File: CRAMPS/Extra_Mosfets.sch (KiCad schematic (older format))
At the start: 12 parts, among them P901 D12, P902 D2, Q901 DMN2075U, Q902 DMN2075U

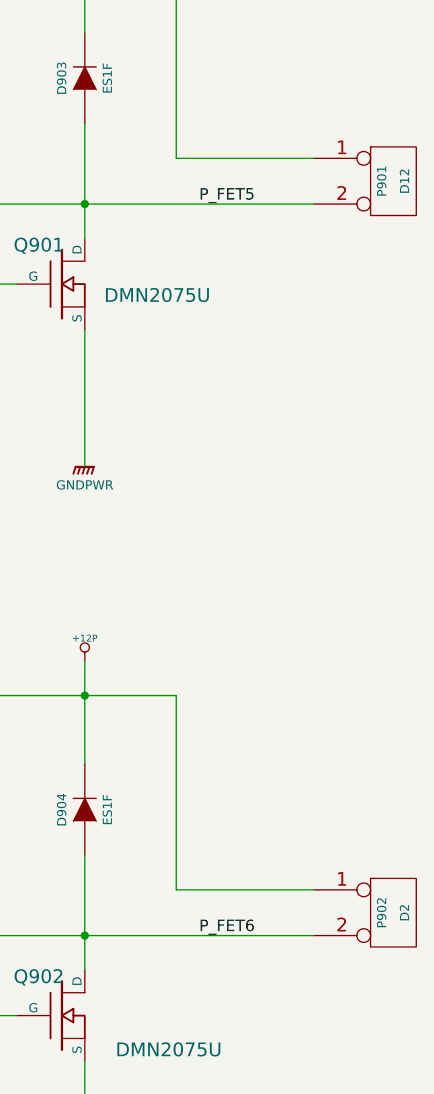
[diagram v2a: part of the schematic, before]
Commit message: P8/P9 Pins assigned, PCB placement in-progress
Signed-off-by: Charles Steinkuehler <charles@steinkuehler.net>
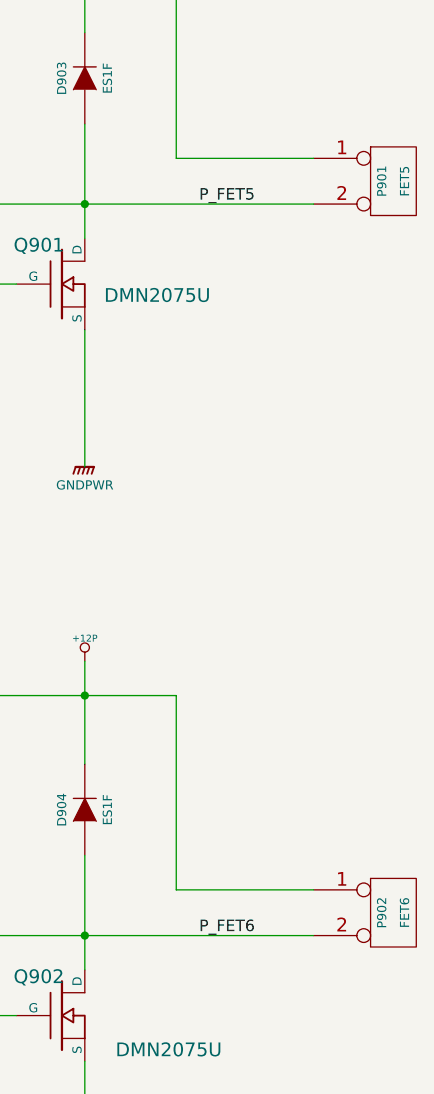
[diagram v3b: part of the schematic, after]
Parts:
- P901: value D12 -> FET5
- P902: value D2 -> FET6
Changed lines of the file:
@@
 Sheet 9 10
 Title "CRAMPS (Cape-RAMPS for BeagleBone)"
-Date "4 feb 2014"
+Date "6 feb 2014"
 Rev "v1.0"
 Comp ""
@@
 P 4850 1950
 F 0 "P901" V 4800 1950 40  0000 C CNN
-F 1 "D12" V 4900 1950 40  0000 C CNN
+F 1 "FET5" V 4900 1950 40  0000 C CNN
 F 2 "" H 4850 1950 60  0001 C CNN
 F 3 "" H 4850 1950 60  0001 C CNN
@@
 P 4850 5150
 F 0 "P902" V 4800 5150 40  0000 C CNN
-F 1 "D2" V 4900 5150 40  0000 C CNN
+F 1 "FET6" V 4900 5150 40  0000 C CNN
 F 2 "" H 4850 5150 60  0001 C CNN
 F 3 "" H 4850 5150 60  0001 C CNN

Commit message: Initial BOM files for PCB version 1.0 Added README and ToDo text files
Signed-off-by: Charles Steinkuehler <charles@steinkuehler.net>
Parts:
- D901, D902: Mfg (none) -> Osram; PartNo (none) -> LH R974-LP-1
- D903, D904: Mfg (none) -> Fairchild; PartNo (none) -> ES1F
- P901, P902: Mfg (none) -> Molex; PartNo (none) -> 22-23-2021
- Q901, Q902: Mfg (none) -> Diodes Inc.; PartNo (none) -> DMN2075U-7
- R901, R902: Mfg (none) -> KOA; PartNo (none) -> RK73H2ATTD2200F
- R905, R906: Mfg (none) -> KOA; PartNo (none) -> RK73H2ATTD1801F
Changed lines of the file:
@@
 Sheet 9 10
 Title "CRAMPS (Cape-RAMPS for BeagleBone)"
-Date "9 feb 2014"
+Date "11 feb 2014"
 Rev "v1.0"
 Comp ""
@@
 F 2 "" H 3400 2400 60  0001 C CNN
 F 3 "" H 3400 2400 60  0001 C CNN
+F 4 "Diodes Inc." H 6250 6550 60  0001 C CNN "Mfg"
+F 5 "DMN2075U-7" H 6250 6550 60  0001 C CNN "PartNo"
 	1    3400 2400
 	1    0    0    -1
@@
 F 2 "" H 4850 1950 60  0001 C CNN
 F 3 "" H 4850 1950 60  0001 C CNN
+F 4 "Molex" H 6250 6550 60  0001 C CNN "Mfg"
+F 5 "22-23-2021" H 6250 6550 60  0001 C CNN "PartNo"
 	1    4850 1950
 	1    0    0    -1
@@
 F 2 "" H 3500 1500 60  0001 C CNN
 F 3 "" H 3500 1500 60  0001 C CNN
+F 4 "Fairchild" H 6250 6550 60  0001 C CNN "Mfg"
+F 5 "ES1F" H 6250 6550 60  0001 C CNN "PartNo"
 	1    3500 1500
 	0    -1   -1   0
@@
 F 2 "" H 3000 1800 60  0001 C CNN
 F 3 "" H 3000 1800 60  0001 C CNN
+F 4 "Osram" H 6250 6550 60  0001 C CNN "Mfg"
+F 5 "LH R974-LP-1" H 6250 6550 60  0001 C CNN "PartNo"
 	1    3000 1800
 	0    1    1    0
@@
 F 2 "" H 3000 1300 60  0001 C CNN
 F 3 "" H 3000 1300 60  0001 C CNN
+F 4 "KOA" H 6250 6550 60  0001 C CNN "Mfg"
+F 5 "RK73H2ATTD1801F" H 6250 6550 60  0001 C CNN "PartNo"
 	1    3000 1300
 	1    0    0    -1
@@
 F 2 "" H 3400 5600 60  0001 C CNN
 F 3 "" H 3400 5600 60  0001 C CNN
+F 4 "Diodes Inc." H 6250 6550 60  0001 C CNN "Mfg"
+F 5 "DMN2075U-7" H 6250 6550 60  0001 C CNN "PartNo"
 	1    3400 5600
 	1    0    0    -1
@@
 F 2 "" H 4850 5150 60  0001 C CNN
 F 3 "" H 4850 5150 60  0001 C CNN
+F 4 "Molex" H 6250 6550 60  0001 C CNN "Mfg"
+F 5 "22-23-2021" H 6250 6550 60  0001 C CNN "PartNo"
 	1    4850 5150
 	1    0    0    -1
@@
 F 2 "" H 3500 4700 60  0001 C CNN
 F 3 "" H 3500 4700 60  0001 C CNN
+F 4 "Fairchild" H 6250 6550 60  0001 C CNN "Mfg"
+F 5 "ES1F" H 6250 6550 60  0001 C CNN "PartNo"
 	1    3500 4700
 	0    -1   -1   0
@@
 F 2 "" H 3000 5000 60  0001 C CNN
 F 3 "" H 3000 5000 60  0001 C CNN
+F 4 "Osram" H 6250 6550 60  0001 C CNN "Mfg"
+F 5 "LH R974-LP-1" H 6250 6550 60  0001 C CNN "PartNo"
 	1    3000 5000
 	0    1    1    0
@@
 F 2 "" H 3000 4500 60  0001 C CNN
 F 3 "" H 3000 4500 60  0001 C CNN
+F 4 "KOA" H 6250 6550 60  0001 C CNN "Mfg"
+F 5 "RK73H2ATTD1801F" H 6250 6550 60  0001 C CNN "PartNo"
 	1    3000 4500
 	1    0    0    -1
@@
 F 2 "~" V 2080 2400 30  0000 C CNN
 F 3 "~" H 2150 2400 30  0000 C CNN
+F 4 "KOA" H 6250 6550 60  0001 C CNN "Mfg"
+F 5 "RK73H2ATTD2200F" H 6250 6550 60  0001 C CNN "PartNo"
 	1    2150 2400
 	0    -1   -1   0
@@
 F 2 "~" V 2030 5600 30  0000 C CNN
 F 3 "~" H 2100 5600 30  0000 C CNN
+F 4 "KOA" H 6250 6550 60  0001 C CNN "Mfg"
+F 5 "RK73H2ATTD2200F" H 6250 6550 60  0001 C CNN "PartNo"
 	1    2100 5600
 	0    -1   -1   0

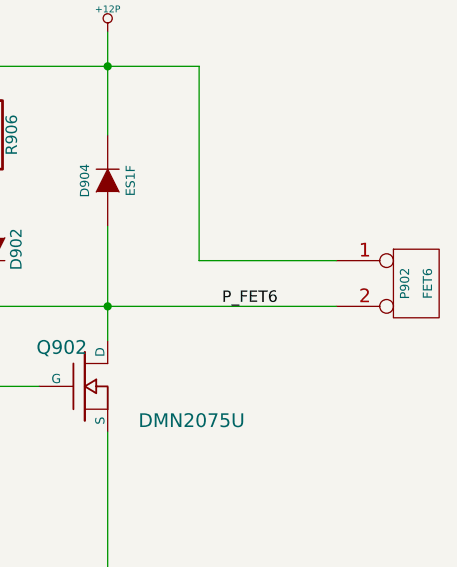
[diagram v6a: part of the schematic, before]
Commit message: BOM Updates Fixed incorrect Molex part number Added Stackpole resistor part numbers Switched to value-sorted BOM export from KiCAD Modified some attribute fields to get same-value parts to list on a single BOM line
Signed-off-by: Charles Steinkuehler <charles@steinkuehler.net>
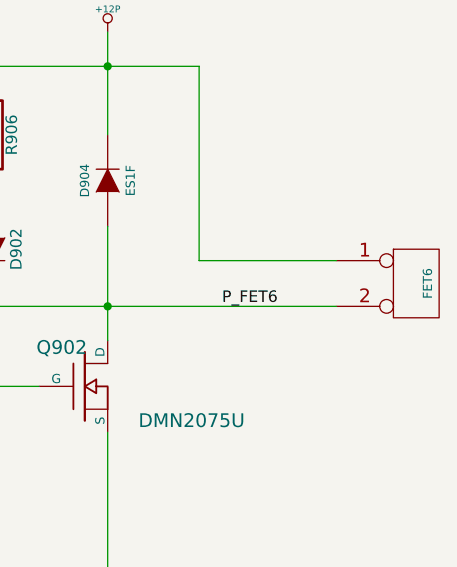
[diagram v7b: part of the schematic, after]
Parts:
- R901, R902: footprint ~ -> (none); AltMfg (none) -> KOA; AltPartNo (none) -> RK73H2ATTD2200F; Mfg KOA -> Stackpole; PartNo RK73H2ATTD2200F -> RMCF0805FT220R
- R905, R906: AltMfg (none) -> KOA; AltPartNo (none) -> RK73H2ATTD1801F; Mfg KOA -> Stackpole; PartNo RK73H2ATTD1801F -> RMCF0805FT1K80
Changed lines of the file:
@@
 Sheet 9 10
 Title "CRAMPS (Cape-RAMPS for BeagleBone)"
-Date "11 feb 2014"
+Date "15 feb 2014"
 Rev "v1.0"
 Comp ""
@@
 Connection ~ 3500 1000
 Wire Wire Line
-	3000 1000 3900 1000
-Wire Wire Line
-	3500 3200 3500 2600
-Wire Wire Line
-	3000 2050 4500 2050
-Wire Wire Line
-	3000 2050 3000 2000
-Wire Wire Line
-	3000 1600 3000 1550
+    3000 1000 3900 1000
+Wire Wire Line
+    3500 3200 3500 2600
+Wire Wire Line
+    3000 2050 4500 2050
+Wire Wire Line
+    3000 2050 3000 2000
+Wire Wire Line
+    3000 1600 3000 1550
 Connection ~ 3500 2050
 Wire Wire Line
-	3500 1700 3500 2200
-Wire Wire Line
-	3000 1000 3000 1050
-Wire Wire Line
-	4500 1850 3900 1850
-Wire Wire Line
-	3900 1850 3900 1000
-Wire Wire Line
-	3500 850  3500 1300
+    3500 1700 3500 2200
+Wire Wire Line
+    3000 1000 3000 1050
+Wire Wire Line
+    4500 1850 3900 1850
+Wire Wire Line
+    3900 1850 3900 1000
+Wire Wire Line
+    3500 850  3500 1300
 $Comp
 L MOS_N Q901
@@
 F 4 "Diodes Inc." H 6250 6550 60  0001 C CNN "Mfg"
 F 5 "DMN2075U-7" H 6250 6550 60  0001 C CNN "PartNo"
-	1    3400 2400
-	1    0    0    -1
+    1    3400 2400
+    1    0    0    -1
 $EndComp
 $Comp
@@
 F 2 "" H 3500 3200 60  0001 C CNN
 F 3 "" H 3500 3200 60  0001 C CNN
-	1    3500 3200
-	1    0    0    -1
+    1    3500 3200
+    1    0    0    -1
 $EndComp
 $Comp
@@
 F 4 "Molex" H 6250 6550 60  0001 C CNN "Mfg"
 F 5 "22-23-2021" H 6250 6550 60  0001 C CNN "PartNo"
-	1    4850 1950
-	1    0    0    -1
+    1    4850 1950
+    1    0    0    -1
 $EndComp
 $Comp
@@
 F 4 "Fairchild" H 6250 6550 60  0001 C CNN "Mfg"
 F 5 "ES1F" H 6250 6550 60  0001 C CNN "PartNo"
-	1    3500 1500
-	0    -1   -1   0
+    1    3500 1500
+    0    -1   -1   0
 $EndComp
 $Comp
@@
 F 4 "Osram" H 6250 6550 60  0001 C CNN "Mfg"
 F 5 "LH R974-LP-1" H 6250 6550 60  0001 C CNN "PartNo"
-	1    3000 1800
-	0    1    1    0
+    1    3000 1800
+    0    1    1    0
 $EndComp
 $Comp
@@
 F 2 "" H 3000 1300 60  0001 C CNN
 F 3 "" H 3000 1300 60  0001 C CNN
-F 4 "KOA" H 6250 6550 60  0001 C CNN "Mfg"
-F 5 "RK73H2ATTD1801F" H 6250 6550 60  0001 C CNN "PartNo"
-	1    3000 1300
-	1    0    0    -1
+F 4 "Stackpole" H 6250 6550 60  0001 C CNN "Mfg"
+F 5 "RMCF0805FT1K80" H 6250 6550 60  0001 C CNN "PartNo"
+F 6 "KOA" H 6250 6550 60  0001 C CNN "AltMfg"
+F 7 "RK73H2ATTD1801F" H 6250 6550 60  0001 C CNN "AltPartNo"
+    1    3000 1300
+    1    0    0    -1
 $EndComp
 Text GLabel 1450 2400 0    60   Input ~ 0
@@
 F 2 "" H 3500 850 60  0000 C CNN
 F 3 "" H 3500 850 60  0000 C CNN
-	1    3500 850
-	1    0    0    -1
+    1    3500 850
+    1    0    0    -1
 $EndComp
 Text Label 4000 2050 0    50   ~ 0
@@
 Connection ~ 3500 4200
 Wire Wire Line
-	3000 4200 3900 4200
-Wire Wire Line
-	3500 6400 3500 5800
-Wire Wire Line
-	3000 5250 4500 5250
-Wire Wire Line
-	3000 5250 3000 5200
-Wire Wire Line
-	3000 4800 3000 4750
+    3000 4200 3900 4200
+Wire Wire Line
+    3500 6400 3500 5800
+Wire Wire Line
+    3000 5250 4500 5250
+Wire Wire Line
+    3000 5250 3000 5200
+Wire Wire Line
+    3000 4800 3000 4750
 Connection ~ 3500 5250
 Wire Wire Line
-	3500 4900 3500 5400
-Wire Wire Line
-	3000 4200 3000 4250
-Wire Wire Line
-	4500 5050 3900 5050
-Wire Wire Line
-	3900 5050 3900 4200
-Wire Wire Line
-	3500 4050 3500 4500
+    3500 4900 3500 5400
+Wire Wire Line
+    3000 4200 3000 4250
+Wire Wire Line
+    4500 5050 3900 5050
+Wire Wire Line
+    3900 5050 3900 4200
+Wire Wire Line
+    3500 4050 3500 4500
 $Comp
 L MOS_N Q902
@@
 F 4 "Diodes Inc." H 6250 6550 60  0001 C CNN "Mfg"
 F 5 "DMN2075U-7" H 6250 6550 60  0001 C CNN "PartNo"
-	1    3400 5600
-	1    0    0    -1
+    1    3400 5600
+    1    0    0    -1
 $EndComp
 $Comp
@@
 F 2 "" H 3500 6400 60  0001 C CNN
 F 3 "" H 3500 6400 60  0001 C CNN
-	1    3500 6400
-	1    0    0    -1
+    1    3500 6400
+    1    0    0    -1
 $EndComp
 $Comp
@@
 U 1 1 523E66B1
 P 4850 5150
-F 0 "P902" V 4800 5150 40  0000 C CNN
+F 0 "" V 4800 5150 40  0000 C CNN
 F 1 "FET6" V 4900 5150 40  0000 C CNN
 F 2 "" H 4850 5150 60  0001 C CNN
@@
 F 4 "Molex" H 6250 6550 60  0001 C CNN "Mfg"
 F 5 "22-23-2021" H 6250 6550 60  0001 C CNN "PartNo"
-	1    4850 5150
-	1    0    0    -1
+    1    4850 5150
+    1    0    0    -1
 $EndComp
 $Comp
@@
 F 4 "Fairchild" H 6250 6550 60  0001 C CNN "Mfg"
 F 5 "ES1F" H 6250 6550 60  0001 C CNN "PartNo"
-	1    3500 4700
-	0    -1   -1   0
+    1    3500 4700
+    0    -1   -1   0
 $EndComp
 $Comp
@@
 F 4 "Osram" H 6250 6550 60  0001 C CNN "Mfg"
 F 5 "LH R974-LP-1" H 6250 6550 60  0001 C CNN "PartNo"
-	1    3000 5000
-	0    1    1    0
+    1    3000 5000
+    0    1    1    0
 $EndComp
 $Comp
@@
 F 2 "" H 3000 4500 60  0001 C CNN
 F 3 "" H 3000 4500 60  0001 C CNN
-F 4 "KOA" H 6250 6550 60  0001 C CNN "Mfg"
-F 5 "RK73H2ATTD1801F" H 6250 6550 60  0001 C CNN "PartNo"
-	1    3000 4500
-	1    0    0    -1
+F 4 "Stackpole" H 6250 6550 60  0001 C CNN "Mfg"
+F 5 "RMCF0805FT1K80" H 6250 6550 60  0001 C CNN "PartNo"
+F 6 "KOA" H 6250 6550 60  0001 C CNN "AltMfg"
+F 7 "RK73H2ATTD1801F" H 6250 6550 60  0001 C CNN "AltPartNo"
+    1    3000 4500
+    1    0    0    -1
 $EndComp
 Text GLabel 1450 5600 0    60   Input ~ 0
@@
 F 2 "" H 3500 4050 60  0000 C CNN
 F 3 "" H 3500 4050 60  0000 C CNN
-	1    3500 4050
-	1    0    0    -1
+    1    3500 4050
+    1    0    0    -1
 $EndComp
 Text Label 4000 5250 0    50   ~ 0
@@
 F 0 "R902" V 2230 2400 40  0000 C CNN
 F 1 "220R" V 2157 2401 40  0000 C CNN
-F 2 "~" V 2080 2400 30  0000 C CNN
-F 3 "~" H 2150 2400 30  0000 C CNN
-F 4 "KOA" H 6250 6550 60  0001 C CNN "Mfg"
-F 5 "RK73H2ATTD2200F" H 6250 6550 60  0001 C CNN "PartNo"
-	1    2150 2400
-	0    -1   -1   0
-$EndComp
-Wire Wire Line
-	1900 2400 1450 2400
-Wire Wire Line
-	2400 2400 3200 2400
+F 2 "" V 2080 2400 30  0000 C CNN
+F 3 "" H 2150 2400 30  0000 C CNN
+F 4 "Stackpole" H 6250 6550 60  0001 C CNN "Mfg"
+F 5 "RMCF0805FT220R" H 6250 6550 60  0001 C CNN "PartNo"
+F 6 "KOA" H 6250 6550 60  0001 C CNN "AltMfg"
+F 7 "RK73H2ATTD2200F" H 6250 6550 60  0001 C CNN "AltPartNo"
+    1    2150 2400
+    0    -1   -1   0
+$EndComp
+Wire Wire Line
+    1900 2400 1450 2400
+Wire Wire Line
+    2400 2400 3200 2400
 $Comp
 L R R901
@@
 F 0 "R901" V 2180 5600 40  0000 C CNN
 F 1 "220R" V 2107 5601 40  0000 C CNN
-F 2 "~" V 2030 5600 30  0000 C CNN
-F 3 "~" H 2100 5600 30  0000 C CNN
-F 4 "KOA" H 6250 6550 60  0001 C CNN "Mfg"
-F 5 "RK73H2ATTD2200F" H 6250 6550 60  0001 C CNN "PartNo"
-	1    2100 5600
-	0    -1   -1   0
-$EndComp
-Wire Wire Line
-	1850 5600 1450 5600
-Wire Wire Line
-	2350 5600 3200 5600
+F 2 "" V 2030 5600 30  0000 C CNN
+F 3 "" H 2100 5600 30  0000 C CNN
+F 4 "Stackpole" H 6250 6550 60  0001 C CNN "Mfg"
+F 5 "RMCF0805FT220R" H 6250 6550 60  0001 C CNN "PartNo"
+F 6 "KOA" H 6250 6550 60  0001 C CNN "AltMfg"
+F 7 "RK73H2ATTD2200F" H 6250 6550 60  0001 C CNN "AltPartNo"
+    1    2100 5600
+    0    -1   -1   0
+$EndComp
+Wire Wire Line
+    1850 5600 1450 5600
+Wire Wire Line
+    2350 5600 3200 5600
 $EndSCHEMATC

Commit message: Add note indicating standard pin headers can be used for BeagleBone if additional cape expansion is not required
Signed-off-by: Charles Steinkuehler <charles@steinkuehler.net>
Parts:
- renumbered P902 to P
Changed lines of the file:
@@
 Sheet 9 10
 Title "CRAMPS (Cape-RAMPS for BeagleBone)"
-Date "15 feb 2014"
+Date "17 feb 2014"
 Rev "v1.0"
 Comp ""
@@
 Connection ~ 3500 1000
 Wire Wire Line
-    3000 1000 3900 1000
-Wire Wire Line
-    3500 3200 3500 2600
-Wire Wire Line
-    3000 2050 4500 2050
-Wire Wire Line
-    3000 2050 3000 2000
-Wire Wire Line
-    3000 1600 3000 1550
+	3000 1000 3900 1000
+Wire Wire Line
+	3500 3200 3500 2600
+Wire Wire Line
+	3000 2050 4500 2050
+Wire Wire Line
+	3000 2050 3000 2000
+Wire Wire Line
+	3000 1600 3000 1550
 Connection ~ 3500 2050
 Wire Wire Line
-    3500 1700 3500 2200
-Wire Wire Line
-    3000 1000 3000 1050
-Wire Wire Line
-    4500 1850 3900 1850
-Wire Wire Line
-    3900 1850 3900 1000
-Wire Wire Line
-    3500 850  3500 1300
+	3500 1700 3500 2200
+Wire Wire Line
+	3000 1000 3000 1050
+Wire Wire Line
+	4500 1850 3900 1850
+Wire Wire Line
+	3900 1850 3900 1000
+Wire Wire Line
+	3500 850  3500 1300
 $Comp
 L MOS_N Q901
@@
 F 4 "Diodes Inc." H 6250 6550 60  0001 C CNN "Mfg"
 F 5 "DMN2075U-7" H 6250 6550 60  0001 C CNN "PartNo"
-    1    3400 2400
-    1    0    0    -1
+	1    3400 2400
+	1    0    0    -1
 $EndComp
 $Comp
@@
 F 2 "" H 3500 3200 60  0001 C CNN
 F 3 "" H 3500 3200 60  0001 C CNN
-    1    3500 3200
-    1    0    0    -1
+	1    3500 3200
+	1    0    0    -1
 $EndComp
 $Comp
@@
 F 4 "Molex" H 6250 6550 60  0001 C CNN "Mfg"
 F 5 "22-23-2021" H 6250 6550 60  0001 C CNN "PartNo"
-    1    4850 1950
-    1    0    0    -1
+	1    4850 1950
+	1    0    0    -1
 $EndComp
 $Comp
@@
 F 4 "Fairchild" H 6250 6550 60  0001 C CNN "Mfg"
 F 5 "ES1F" H 6250 6550 60  0001 C CNN "PartNo"
-    1    3500 1500
-    0    -1   -1   0
+	1    3500 1500
+	0    -1   -1   0
 $EndComp
 $Comp
@@
 F 4 "Osram" H 6250 6550 60  0001 C CNN "Mfg"
 F 5 "LH R974-LP-1" H 6250 6550 60  0001 C CNN "PartNo"
-    1    3000 1800
-    0    1    1    0
+	1    3000 1800
+	0    1    1    0
 $EndComp
 $Comp
@@
 F 6 "KOA" H 6250 6550 60  0001 C CNN "AltMfg"
 F 7 "RK73H2ATTD1801F" H 6250 6550 60  0001 C CNN "AltPartNo"
-    1    3000 1300
-    1    0    0    -1
+	1    3000 1300
+	1    0    0    -1
 $EndComp
 Text GLabel 1450 2400 0    60   Input ~ 0
@@
 F 2 "" H 3500 850 60  0000 C CNN
 F 3 "" H 3500 850 60  0000 C CNN
-    1    3500 850
-    1    0    0    -1
+	1    3500 850
+	1    0    0    -1
 $EndComp
 Text Label 4000 2050 0    50   ~ 0
@@
 Connection ~ 3500 4200
 Wire Wire Line
-    3000 4200 3900 4200
-Wire Wire Line
-    3500 6400 3500 5800
-Wire Wire Line
-    3000 5250 4500 5250
-Wire Wire Line
-    3000 5250 3000 5200
-Wire Wire Line
-    3000 4800 3000 4750
+	3000 4200 3900 4200
+Wire Wire Line
+	3500 6400 3500 5800
+Wire Wire Line
+	3000 5250 4500 5250
+Wire Wire Line
+	3000 5250 3000 5200
+Wire Wire Line
+	3000 4800 3000 4750
 Connection ~ 3500 5250
 Wire Wire Line
-    3500 4900 3500 5400
-Wire Wire Line
-    3000 4200 3000 4250
-Wire Wire Line
-    4500 5050 3900 5050
-Wire Wire Line
-    3900 5050 3900 4200
-Wire Wire Line
-    3500 4050 3500 4500
+	3500 4900 3500 5400
+Wire Wire Line
+	3000 4200 3000 4250
+Wire Wire Line
+	4500 5050 3900 5050
+Wire Wire Line
+	3900 5050 3900 4200
+Wire Wire Line
+	3500 4050 3500 4500
 $Comp
 L MOS_N Q902
@@
 F 4 "Diodes Inc." H 6250 6550 60  0001 C CNN "Mfg"
 F 5 "DMN2075U-7" H 6250 6550 60  0001 C CNN "PartNo"
-    1    3400 5600
-    1    0    0    -1
+	1    3400 5600
+	1    0    0    -1
 $EndComp
 $Comp
@@
 F 2 "" H 3500 6400 60  0001 C CNN
 F 3 "" H 3500 6400 60  0001 C CNN
-    1    3500 6400
-    1    0    0    -1
-$EndComp
-$Comp
-L CONN_2 P902
+	1    3500 6400
+	1    0    0    -1
+$EndComp
+$Comp
+L CONN_2 P
 U 1 1 523E66B1
 P 4850 5150
@@
 F 4 "Molex" H 6250 6550 60  0001 C CNN "Mfg"
 F 5 "22-23-2021" H 6250 6550 60  0001 C CNN "PartNo"
-    1    4850 5150
-    1    0    0    -1
+	1    4850 5150
+	1    0    0    -1
 $EndComp
 $Comp
@@
 F 4 "Fairchild" H 6250 6550 60  0001 C CNN "Mfg"
 F 5 "ES1F" H 6250 6550 60  0001 C CNN "PartNo"
-    1    3500 4700
-    0    -1   -1   0
+	1    3500 4700
+	0    -1   -1   0
 $EndComp
 $Comp
@@
 F 4 "Osram" H 6250 6550 60  0001 C CNN "Mfg"
 F 5 "LH R974-LP-1" H 6250 6550 60  0001 C CNN "PartNo"
-    1    3000 5000
-    0    1    1    0
+	1    3000 5000
+	0    1    1    0
 $EndComp
 $Comp
@@
 F 6 "KOA" H 6250 6550 60  0001 C CNN "AltMfg"
 F 7 "RK73H2ATTD1801F" H 6250 6550 60  0001 C CNN "AltPartNo"
-    1    3000 4500
-    1    0    0    -1
+	1    3000 4500
+	1    0    0    -1
 $EndComp
 Text GLabel 1450 5600 0    60   Input ~ 0
@@
 F 2 "" H 3500 4050 60  0000 C CNN
 F 3 "" H 3500 4050 60  0000 C CNN
-    1    3500 4050
-    1    0    0    -1
+	1    3500 4050
+	1    0    0    -1
 $EndComp
 Text Label 4000 5250 0    50   ~ 0
@@
 F 6 "KOA" H 6250 6550 60  0001 C CNN "AltMfg"
 F 7 "RK73H2ATTD2200F" H 6250 6550 60  0001 C CNN "AltPartNo"
-    1    2150 2400
-    0    -1   -1   0
-$EndComp
-Wire Wire Line
-    1900 2400 1450 2400
-Wire Wire Line
-    2400 2400 3200 2400
+	1    2150 2400
+	0    -1   -1   0
+$EndComp
+Wire Wire Line
+	1900 2400 1450 2400
+Wire Wire Line
+	2400 2400 3200 2400
 $Comp
 L R R901
@@
 F 6 "KOA" H 6250 6550 60  0001 C CNN "AltMfg"
 F 7 "RK73H2ATTD2200F" H 6250 6550 60  0001 C CNN "AltPartNo"
-    1    2100 5600
-    0    -1   -1   0
-$EndComp
-Wire Wire Line
-    1850 5600 1450 5600
-Wire Wire Line
-    2350 5600 3200 5600
+	1    2100 5600
+	0    -1   -1   0
+$EndComp
+Wire Wire Line
+	1850 5600 1450 5600
+Wire Wire Line
+	2350 5600 3200 5600
 $EndSCHEMATC
